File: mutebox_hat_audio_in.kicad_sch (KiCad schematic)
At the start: 38 parts, among them J1 GPIO, J3 RCJ-042, J4 RCJ-042, U2 74LVC157, U3 PCM1862DBT, Y3 XO32

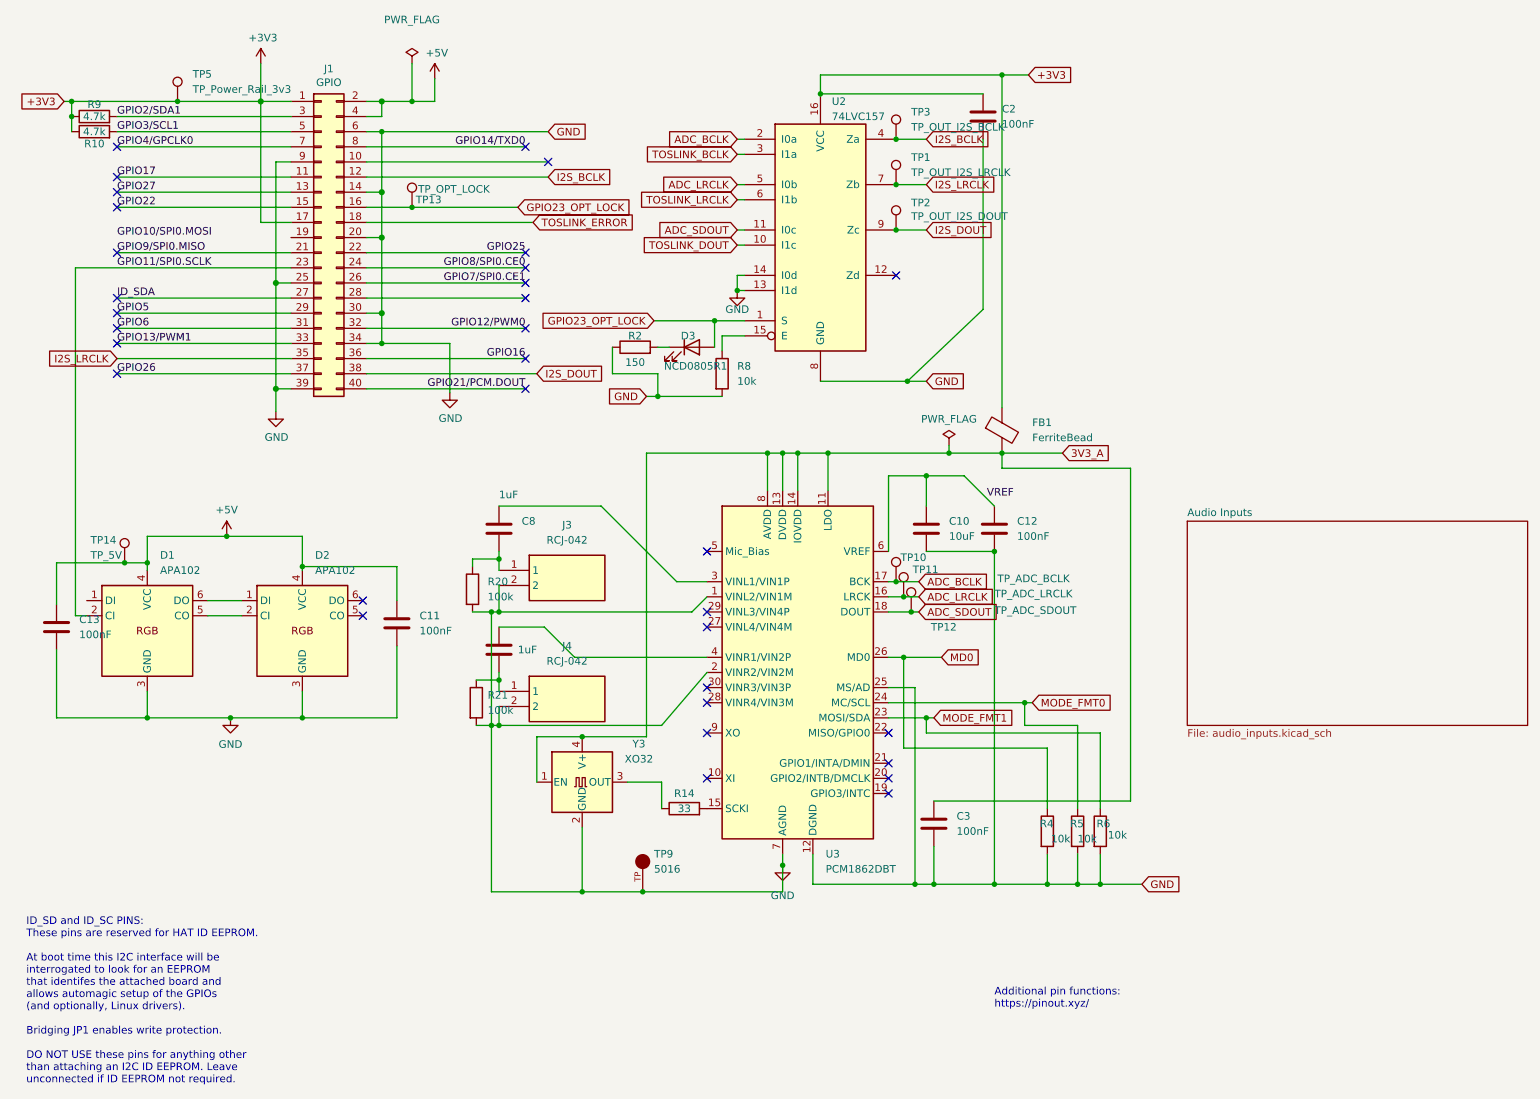
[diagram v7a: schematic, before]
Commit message: Running pins 27-30 to ground through 100k resistors
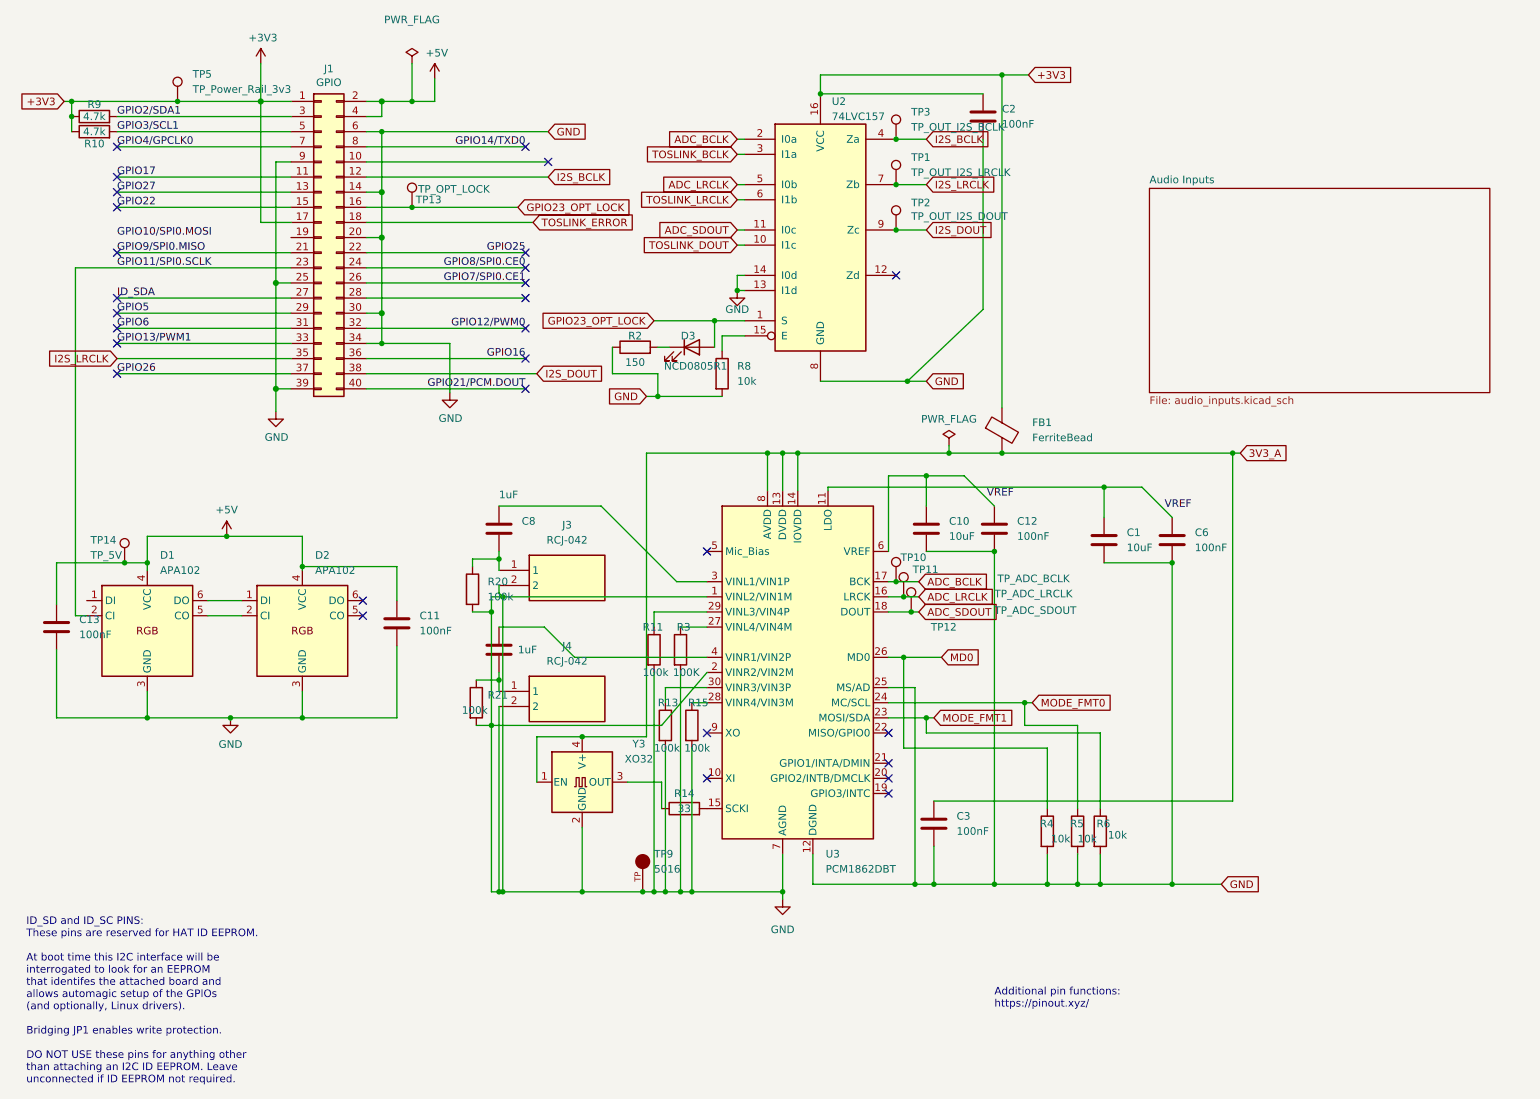
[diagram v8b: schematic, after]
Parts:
- added C1: 10uF, Capacitor_SMD:C_0805_2012Metric_Pad1.18x1.45mm_HandSolder, symbol Device:C
- added C6: 100nF, Capacitor_SMD:C_0805_2012Metric_Pad1.18x1.45mm_HandSolder, symbol Device:C
- added R11, R13, R15: 100k, symbol Device:R
- added R3: 100K, symbol Device:R
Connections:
- net 3V3_A: no longer U3.11 (LDO)
- net GND: now also C1.2, C6.2, R11.2, R13.2, R15.2, R3.2
- net VREF: now also U3.11 (LDO), C1.1, C6.1
- net at U3.27 (VINL4/VIN4M): now also R3.1
- net at U3.28 (VINR4/VIN3M): now also R15.1
- net at U3.29 (VINL3/VIN4P): now also R11.1
- net at U3.30 (VINR3/VIN3P): now also R13.1
- no-connect marks 33 -> 29
